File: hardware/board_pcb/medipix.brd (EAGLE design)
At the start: 95.4 x 90.3 mm, 104 parts, among them IC1 AVR_XMEGA_A4U44A, IC2 FM25H20, P1 53398-0310, P2 53398-0310, P3 53398-0510, U1 IRF7313, U10 BSS138AKA, U11 IRF7313, U12 BSS138AKA, U13 BSS138AKA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

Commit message: Medipix readout working properly
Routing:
- net N$11: track 50.6 -> 41.0 mm
- net +3.3V: track 221.9 -> 216.3 mm
- net N$10: track 45.7 -> 40.9 mm
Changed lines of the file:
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@@
 <wire x1="17.210309375" y1="69.215" x2="18.34550625" y2="68.079803125" width="0.4064" layer="1"/>
 <wire x1="52.705" y1="27.305" x2="67.564" y2="27.305" width="1.27" layer="1"/>
-<wire x1="70.7136" y1="55.0926" x2="68.0212" y2="57.785" width="1.27" layer="1"/>
-<wire x1="74.676" y1="59.055" x2="70.7136" y2="55.0926" width="0.4064" layer="1"/>
+<wire x1="71.247" y1="54.5592" x2="68.0212" y2="57.785" width="1.27" layer="1"/>
 <wire x1="71.247" y1="30.988" x2="71.247" y2="54.5592" width="1.27" layer="1"/>
-<wire x1="71.247" y1="54.5592" x2="70.7136" y2="55.0926" width="1.27" layer="1"/>
 <wire x1="67.564" y1="27.305" x2="71.247" y2="30.988" width="1.27" layer="1"/>
 <contactref element="IC1" pad="39"/>
@@
 <wire x1="61.595" y1="78.105" x2="61.595" y2="76.2" width="0.4064" layer="1"/>
 <wire x1="61.595" y1="75.565" x2="61.595" y2="76.2" width="0.4064" layer="1"/>
-<wire x1="61.595" y1="78.105" x2="62.23" y2="78.74" width="0.4064" layer="1"/>
-<wire x1="62.23" y1="78.74" x2="66.136" y2="78.74" width="0.4064" layer="1"/>
 </signal>
 <signal name="N$11">
@@
 <wire x1="59.055" y1="78.105" x2="59.055" y2="76.2" width="0.4064" layer="1"/>
 <wire x1="59.055" y1="76.2" x2="59.055" y2="74.93" width="0.4064" layer="1"/>
-<wire x1="59.055" y1="74.93" x2="60.325" y2="73.66" width="0.4064" layer="1"/>
-<wire x1="60.325" y1="73.66" x2="68.136" y2="73.66" width="0.4064" layer="1"/>
 </signal>
 <signal name="PA0">

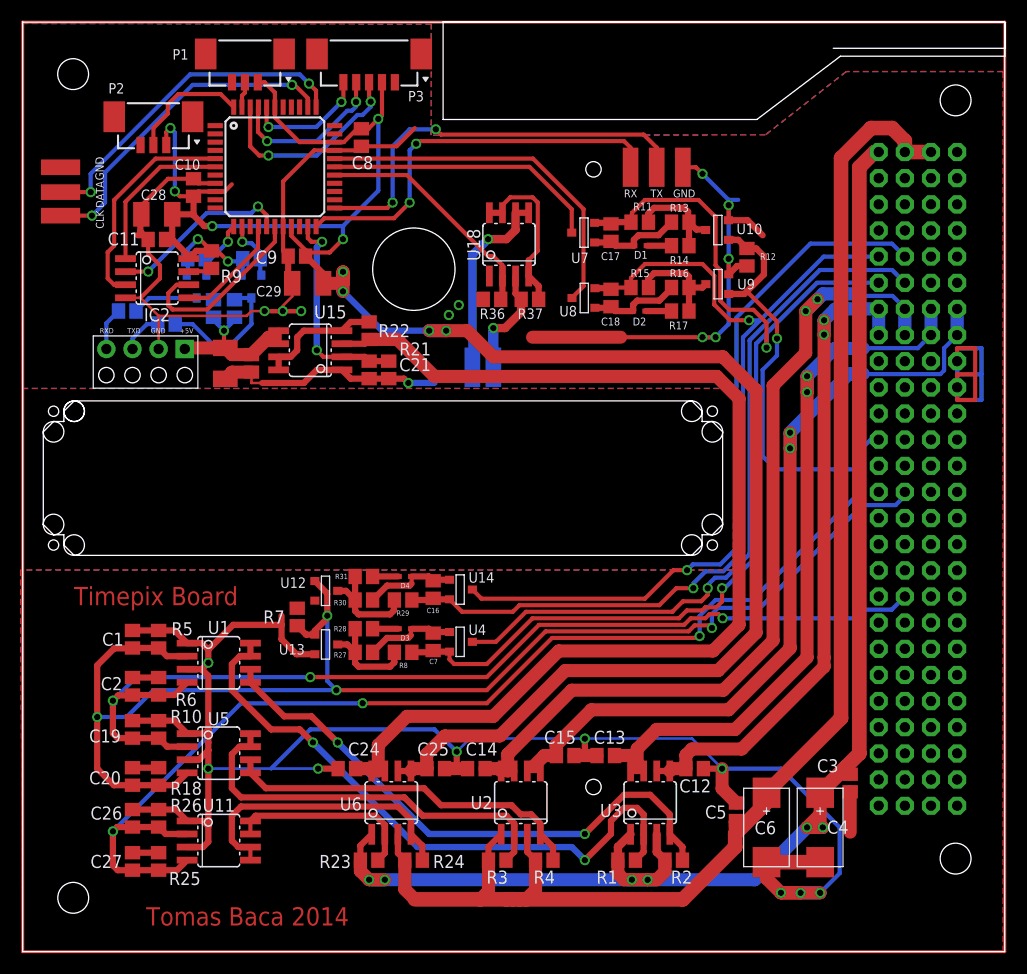
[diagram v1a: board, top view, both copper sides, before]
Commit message: + Board updated with temperature sensor connector
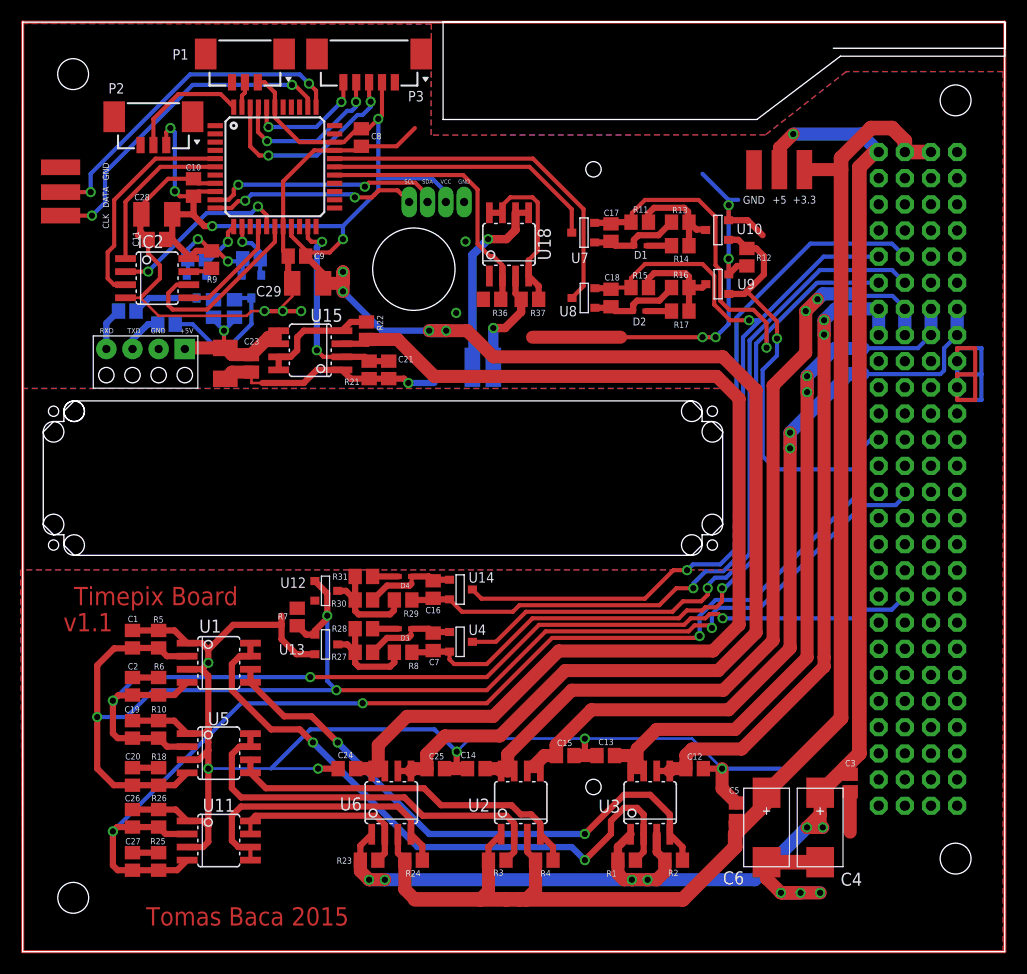
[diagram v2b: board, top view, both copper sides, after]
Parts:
- removed RXD0: RX, medipix:PIN
- removed TXD0: TX, medipix:PIN
- added GND25: +3.3, medipix:PIN
- added GND28: +5, medipix:PIN
- added U$1: THERM, medipix:THERM
- P1, P2: value 53398-0310 -> PICOBLADE
- P3: value 53398-0510 -> PICOBLADE
- moved GND1 6.91 mm to (71.0, 76.0)
- moved R22 0.25 mm to (33.4, 60.3)
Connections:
- removed net N$10: IC1.23, TXD0.P$1
- removed net N$11: IC1.22, RXD0.P$1
- new net GND: U$1.GND
- new net N$12: IC1.11, U$1.SCL
- new net N$13: IC1.10, U$1.SDA
- net +3.3V: now also U$1.VCC
- net +3.3V-IN: now also GND25.P$1
- net +5V-IN: now also GND28.P$1
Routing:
- net N$11: track 41.0 -> 0.00 mm, vias 2 -> 0
- net N$10: track 40.9 -> 0.00 mm, vias 2 -> 0
- net N$13: track 0.00 -> 22.9 mm, vias 0 -> 2
- net GNDD: track 374.0 -> 353.4 mm, vias 20 -> 19
- net N$12: track 0.00 -> 20.3 mm, vias 0 -> 2
- net +5V-IN: track 138.9 -> 152.0 mm, vias 6 -> 7
- net +3.3V: track 216.3 -> 222.5 mm
- net +3.3V-IN: track 143.6 -> 147.1 mm
- net MEDIPIX-SW2: track 23.4 -> 26.5 mm
- net +5V: track 109.8 -> 110.3 mm
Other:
- board text added: "C:/Users/klaxalk/Desktop/maxwellky.bmp"
- board text added: "Tomas Baca 2015"
- board text added: "v1.1"
- board text removed: "Tomas Baca 2014"
